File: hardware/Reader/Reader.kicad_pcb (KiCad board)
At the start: 4 copper layers, 53.3 x 125.1 mm, 126 parts, among them CN1 AHDF15A-KG-TAXB

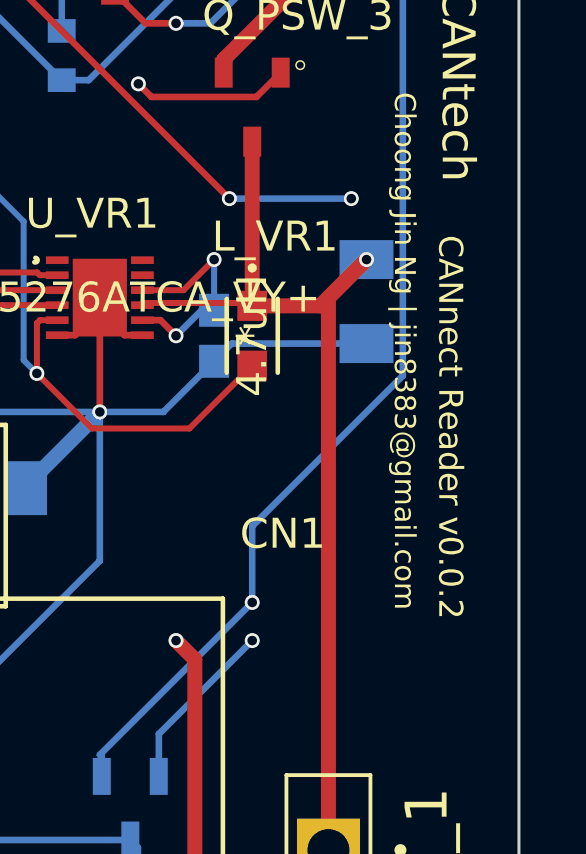
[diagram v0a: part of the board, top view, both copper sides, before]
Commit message: Updated version number for front silkscreen
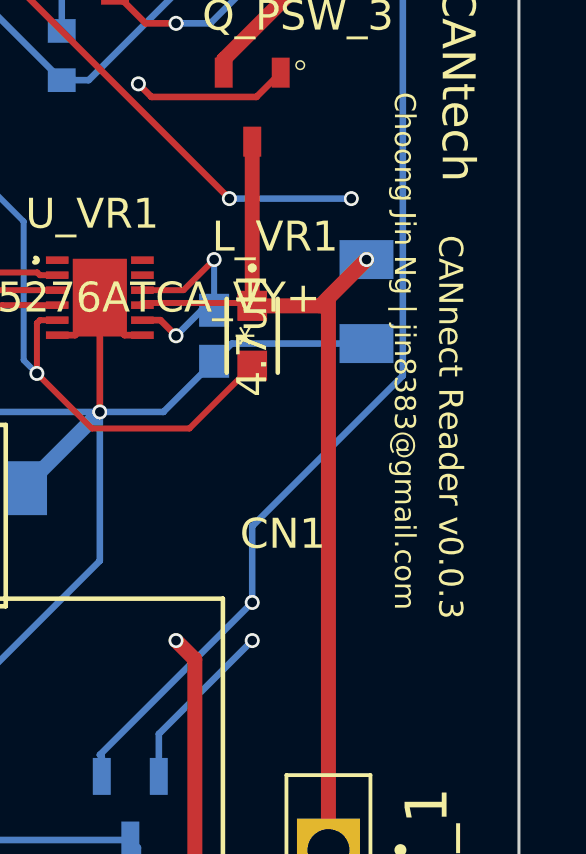
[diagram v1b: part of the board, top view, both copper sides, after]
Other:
- board text added: "CANnect Reader v0.0.3"
- board text removed: "CANnect Reader v0.0.2"
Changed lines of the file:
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@@
     (effects (font (size 1.1 1.1) (thickness 0.15)))
   )
-  (gr_text "CANnect Reader v0.0.2" (at 164.084 145.288 270) (layer F.SilkS)
+  (gr_text "CANnect Reader v0.0.3" (at 164.084 145.288 270) (layer F.SilkS)
     (effects (font (size 0.8 0.8) (thickness 0.15)))
   )

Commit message: Fixed a component name for header pin
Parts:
- C_SWCAN_2: value 4.7uF 25V -> 4.7uF

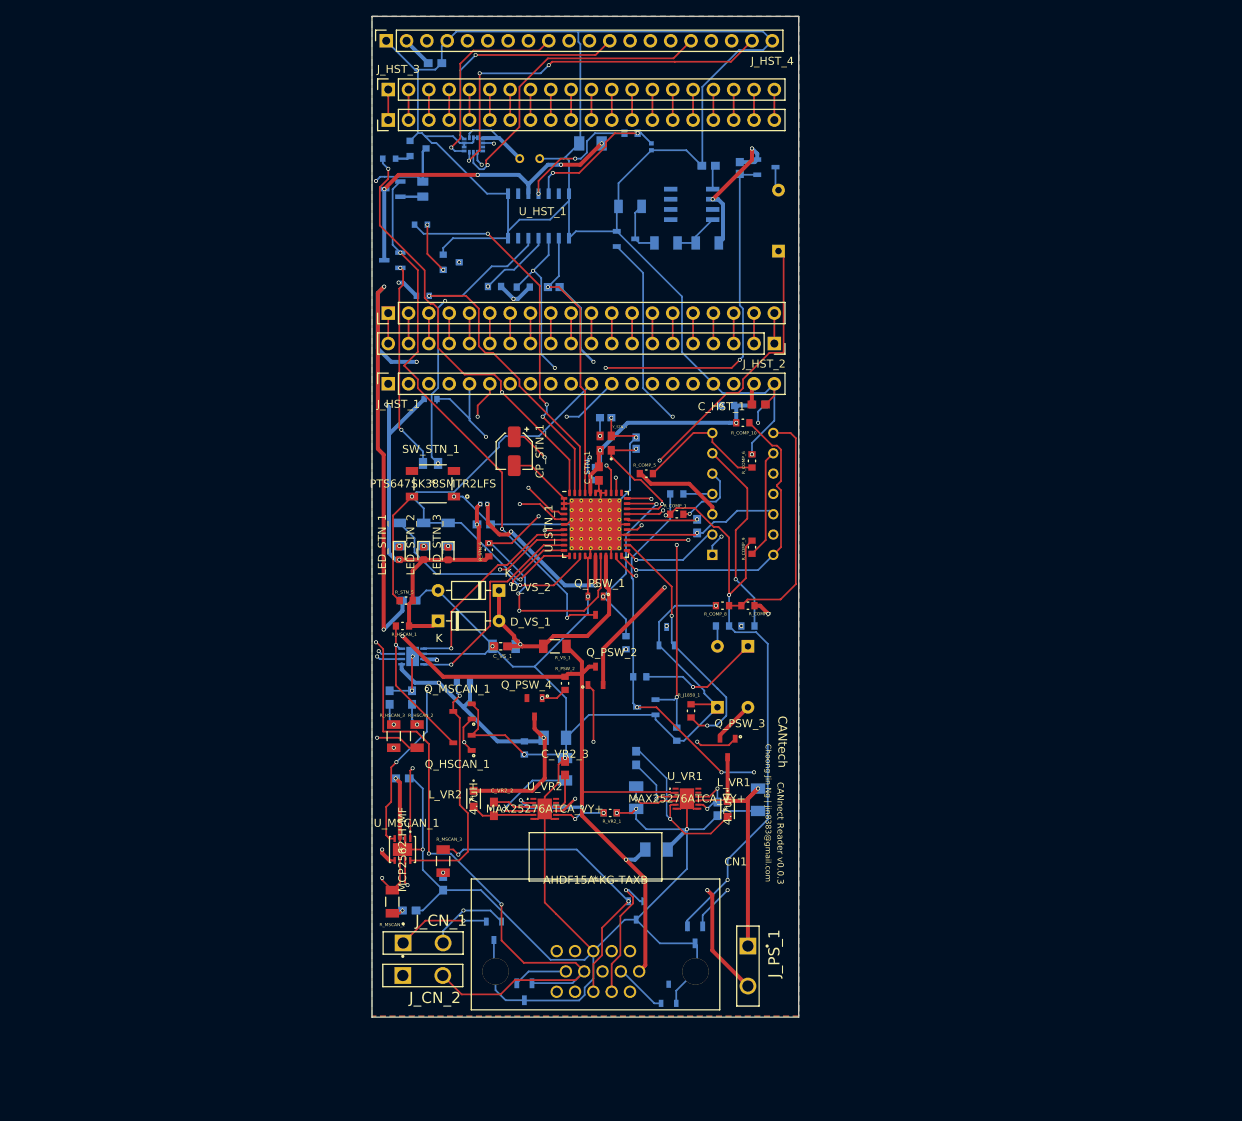
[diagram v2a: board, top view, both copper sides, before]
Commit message: Updated reader schematic to v0.0.5 by adding ESP32, removing unused transceivers, fixed design flaws, increased header pins and fixed footprints. Working on reader PCB design
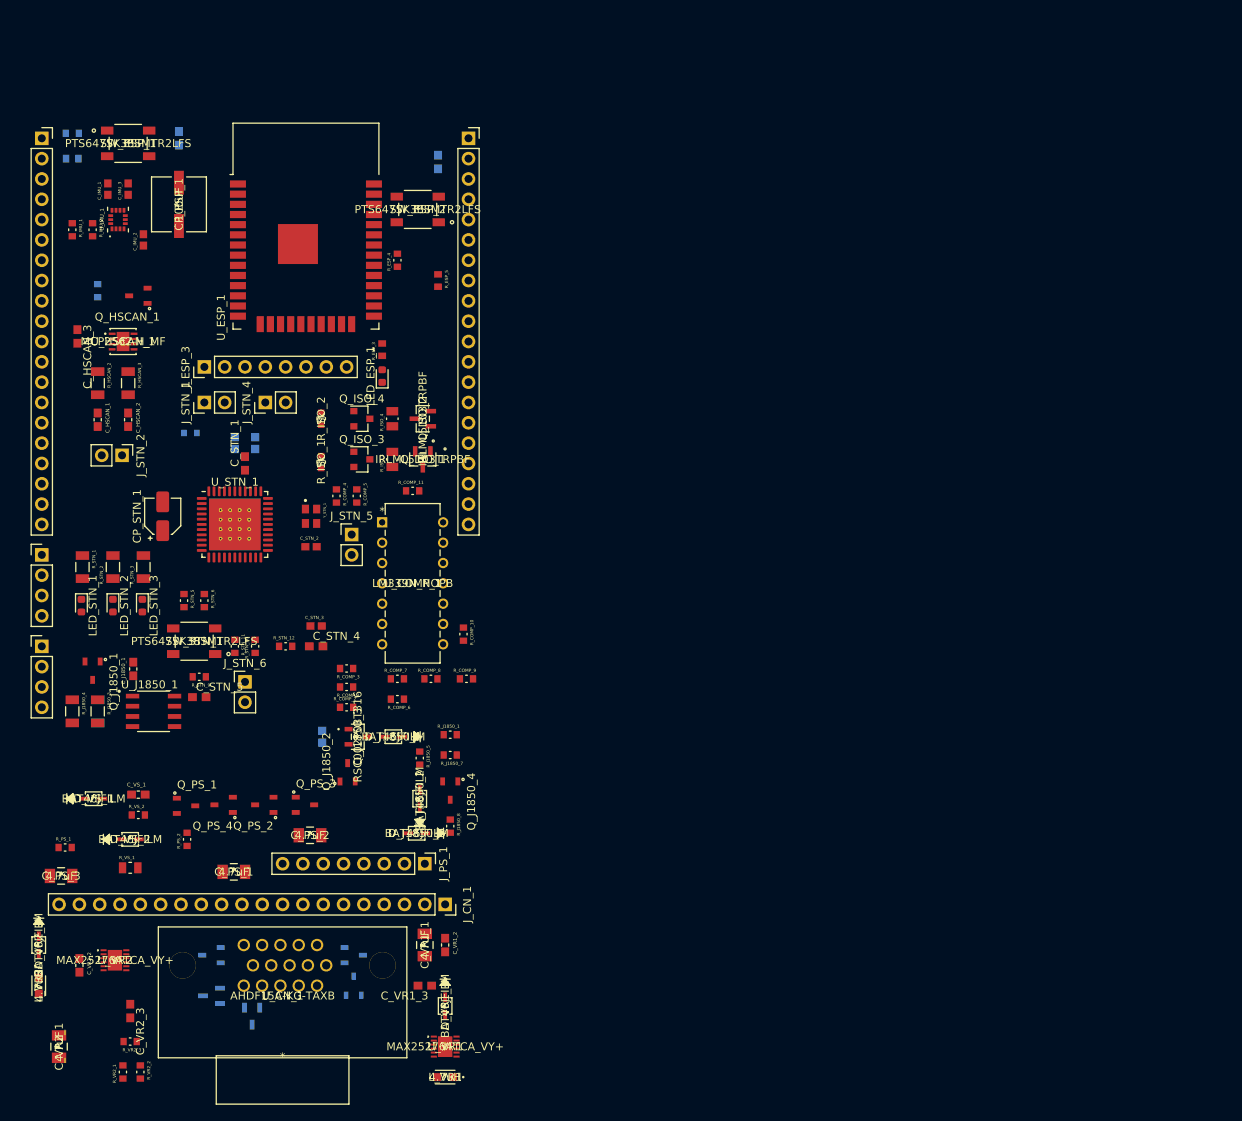
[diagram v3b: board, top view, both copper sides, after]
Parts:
- removed CN1: AHDF15A-KG-TAXB, footprints:AHDF15A-KG-TAXB
- removed C_HST_1, C_HST_2, C_MSCAN_3: 1uF, footprints:0603
- removed C_MM_1: 100nF, footprints:FA16C0G2A104JRU06
- removed C_MSCAN_1, C_MSCAN_2: 560pF, footprints:CAPC1608X90
- removed C_SWCAN_1: 150pF, footprints:CAPC1005X55N
- removed C_SWCAN_2: 4.7uF, footprints:C1206C475K3RACAUTO
- removed J_CN_2: 1546931-2, footprints:1546931-2
- removed J_HST_1, J_HST_2, J_HST_3, J_HST_4: 4157, Connector_PinSocket_2.54mm:PinSocket_1x20_P2.54mm_Vertical
- removed Q_MSCAN_1, Q_PSW_1, Q_PSW_2, Q_PSW_3, Q_PSW_4: NX7002AK,215, footprints:SOT95P230X110-3N
- removed R_COMP1, R_SWCAN_4, R_SWCAN_5: 10k, footprints:RESC1608X55N
- removed R_MSCAN_1, R_PSW_1, R_PSW_2: 100k, footprints:RESC1608X55N
- removed R_MSCAN_2, R_MSCAN_3: 100, footprints:RESC3216X70N
- removed R_SWCAN_3: 6.49k 0.12W, footprints:RESC1608X55N
- removed R_SWCAN_6: 1k, footprints:RC1608F102CS
- removed R_SWCAN_7: 1.5k, footprints:RESC1607X60N
- removed U_HST_1: ESP32_Holder, footprints:ESP32_Holder
- removed U_MM_1: LSM6DSMTR, footprints:PQFN50P300X250X86-14N
- removed U_MSCAN_1: MCP2562-H_MF, footprints:MCP2562-H&slash_MF
- removed U_SWCAN_1: TH8056KDC-AAA-014-RE, footprints:TH8056KDC-AAA-014-RE
- added CP_ESP_1: 100uF, footprints:UCB0J101MCL1GS, F.Cu at (88.9, 66.7)
- added C_ESP_1: 0.1uF, footprints:CAPC1608X90, B.Cu at (88.9, 58.4)
- added C_ESP_2: 0.1uF, footprints:CAPC1608X90, B.Cu at (121.3, 61.4)
- added C_IMU_1: 100nF, footprints:CAPC1608X90N, F.Cu at (80.0, 64.8)
- added C_IMU_2: 100nF, footprints:CAPC1608X90N, F.Cu at (84.5, 71.1)
- added C_IMU_3: 100nF, footprints:CAPC1608X90N, F.Cu at (82.5, 64.8)
- added D_VR1_1: BAT46JFILM, footprints:BAT46JFILM, F.Cu at (122.2, 166.9)
- added D_VR2_1: BAT46JFILM, footprints:BAT46JFILM, F.Cu at (71.4, 159.3)
- added J_ESP_1: 4157, Connector_PinSocket_2.54mm:PinSocket_1x20_P2.54mm_Vertical, F.Cu at (71.8, 58.4)
- added J_ESP_2: 4157, Connector_PinSocket_2.54mm:PinSocket_1x20_P2.54mm_Vertical, F.Cu at (125.1, 58.4)
- added J_ESP_3: Header_Pin_8, Connector_PinHeader_2.54mm:PinHeader_1x08_P2.54mm_Vertical, F.Cu at (92.1, 87.0)
- added J_OBD_1: Header_Pin_4, Connector_PinHeader_2.54mm:PinHeader_1x04_P2.54mm_Vertical, F.Cu at (71.8, 121.9)
- added J_OBD_2: Header_Pin_4, Connector_PinHeader_2.54mm:PinHeader_1x04_P2.54mm_Vertical, F.Cu at (71.8, 110.5)
- added J_STN_1: Header_Pin_2, Connector_PinHeader_2.54mm:PinHeader_1x02_P2.54mm_Vertical, F.Cu at (92.1, 91.4)
- added J_STN_2: Header_Pin_2, Connector_PinHeader_2.54mm:PinHeader_1x02_P2.54mm_Vertical, F.Cu at (81.8, 98.0)
- added J_STN_4: Header_Pin_2, Connector_PinHeader_2.54mm:PinHeader_1x02_P2.54mm_Vertical, F.Cu at (99.7, 91.4)
- added J_STN_5: Header_Pin_2, Connector_PinHeader_2.54mm:PinHeader_1x02_P2.54mm_Vertical, F.Cu at (110.5, 108.0)
- added J_STN_6: Header_Pin_2, Connector_PinHeader_2.54mm:PinHeader_1x02_P2.54mm_Vertical, F.Cu at (97.2, 126.4)
- added LED_ESP_1: LED, LED_SMD:LED_0603_1608Metric, F.Cu at (114.3, 88.1)
- added Q_PS_1: NX7002AK,215, footprints:SOT95P230X110-3N, F.Cu at (89.8, 141.9)
- added Q_PS_2: NX7002AK,215, footprints:SOT95P230X110-3N, F.Cu at (99.6, 141.7)
- added Q_PS_3: NX7002AK,215, footprints:SOT95P230X110-3N, F.Cu at (104.6, 141.7)
- added Q_PS_4: NX7002AK,215, footprints:SOT95P230X110-3N, F.Cu at (94.5, 141.7)
- added R_COMP_11: 10k, footprints:RESC1608X55N, F.Cu at (118.1, 102.5)
- added R_ESP_1: 10k, footprints:RESC1608X55N, B.Cu at (75.6, 57.8)
- added R_ESP_2: 500, footprints:RESC1508X55N, B.Cu at (75.6, 61.0)
- added R_ESP_3: 500, footprints:RESC1508X55N, F.Cu at (114.3, 84.8)
- added R_ESP_4: 10k, footprints:RESC1608X55N, F.Cu at (116.2, 73.7)
- added R_ESP_5: 500, footprints:RESC1508X55N, F.Cu at (121.3, 76.2)
- added R_IMU_1: 4.7k, footprints:RESC1608X55N, F.Cu at (75.6, 69.8)
- added R_IMU_2: 4.7k, footprints:RESC1608X55N, F.Cu at (78.1, 69.8)
- added R_PS_1: 100k, footprints:RESC1608X55N, F.Cu at (74.7, 147.1)
- added R_PS_2: 100k, footprints:RESC1608X55N, F.Cu at (89.9, 146.1)
- added R_STN_10: 10k, footprints:RESC1608X55N, F.Cu at (98.4, 121.9)
- added R_STN_11: 10, footprints:RESC1608X55N, F.Cu at (95.9, 121.9)
- added R_STN_12: 100k, footprints:RESC1608X55N, F.Cu at (102.2, 121.9)
- added R_STN_9: 100k, footprints:RESC1608X55N, F.Cu at (91.4, 125.7)
- added SW_ESP_1: PTS647SK38SMTR2LFS, footprints:PTS647SK38SMTR2LFS, F.Cu at (82.5, 59.1)
- added SW_ESP_2: PTS647SK38SMTR2LFS, footprints:PTS647SK38SMTR2LFS, F.Cu at (118.7, 67.3)
- added U_CN_1: AHDF15A-KG-TAXB, footprints:AHDF15A-KG-TAXB, F.Cu at (101.9, 165.6)
- added U_ESP_1: ESP32-WROOM-32D, footprints:CANtech-ESP32-WROOM-32, F.Cu at (104.8, 72.4)
- added U_IMU_1: LSM6DSMTR, footprints:PQFN50P300X250X86-14N, F.Cu at (81.3, 68.6)
- C_HSCAN_1, C_HSCAN_2, C_HSCAN_3, C_J1850_1, C_PS_1, C_PS_2, C_PS_3, C_STN_2, C_STN_3, C_STN_4, C_STN_5, C_VR1_1, C_VR1_2, C_VR1_3, C_VR2_1, Q_ISO_1, Q_ISO_2, Q_ISO_3, Q_ISO_4, Q_J1850_1, Q_J1850_2, Q_J1850_3, Q_J1850_4, R_COMP_2, R_COMP_3, R_COMP_4, R_ISO_1, R_ISO_2, R_J1850_3, R_J1850_4, R_J1850_5, R_J1850_7, R_J1850_8, R_STN_1, R_STN_2, R_VR2_2, R_VR2_3, U_COMP_1, U_HSCAN_1, U_J1850_1: moved to F.Cu
- D_J1850_1, D_J1850_2, D_J1850_3: value BAT46 -> BAT46JFILM; footprint Diode_THT:D_DO-35_SOD27_P7.62mm_Horizontal -> footprints:BAT46JFILM; moved to F.Cu
- D_VS_1, D_VS_2: value BAT46 -> BAT46JFILM; footprint Diode_THT:D_DO-35_SOD27_P7.62mm_Horizontal -> footprints:BAT46JFILM
- J_CN_1: value 1546931-2 -> 4157; footprint footprints:1546931-2 -> Connector_PinSocket_2.54mm:PinSocket_1x20_P2.54mm_Vertical
- J_PS_1: value 1546931-2 -> Header_Pin_8; footprint footprints:1546931-2 -> Connector_PinHeader_2.54mm:PinHeader_1x08_P2.54mm_Vertical
- LED_STN_1: value "Status" -> Status
- LED_STN_2: value "OBD Activity" -> OBD Activity
- LED_STN_3: value "Host Activity" -> Host Activity
- R_COMP_7: value 2.7k -> 10k
- R_COMP_8: value 10k -> 2.7k
- R_HSCAN_1: moved to B.Cu
- R_ISO_3, R_ISO_4: value 510k/0.5W -> 510k; footprint footprints:RESC2012X70N -> footprints:RESC2012X50N; moved to F.Cu
- R_STN_3: value 1k -> 330; footprint footprints:RC1608F102CS -> footprints:RESC3216X70N; moved to F.Cu
- R_STN_4: value 330 -> 1k; footprint footprints:RESC3216X70N -> footprints:RC1608F102CS
- R_STN_6: value 10k -> 100k
- R_STN_7: value 10 -> 1.5k; footprint footprints:RESC1005X40N -> footprints:RESC1607X60N
- R_STN_8: value 100k -> 1.5k; footprint footprints:RESC1608X55N -> footprints:RESC1607X60N
- R_VS_1: value 62k 1% -> 62k; footprint footprints:RESC3216X70N -> footprints:RESC2012X60N
- R_VS_2: value 10k 1% -> 10k; footprint footprints:RESC3216X70N -> footprints:RESC1608X55N; moved to F.Cu
- U_STN_1: footprint Package_DFN_QFN:QFN-44-1EP_8x8mm_P0.65mm_EP6.45x6.45mm_ThermalVias -> footprints:CANtech-STN2120-QFN-44-1EP_8x8mm
- moved R_J1850_6 96.1 mm to (78.7, 130.0), turned to 270 degrees
- moved C_J1850_1 95.5 mm to (83.2, 124.8), turned to 90 degrees
- moved R_J1850_4 94.0 mm to (75.6, 130.0), turned to 270 degrees
- moved U_J1850_1 92.4 mm to (85.7, 130.0), turned to 0 degrees
- moved R_J1850_3 92.1 mm to (78.7, 130.0), turned to 270 degrees
- moved R_J1850_2 88.2 mm to (106.8, 133.2), turned to 90 degrees
- moved Q_J1850_3 87.6 mm to (111.3, 133.2), turned to 270 degrees
- moved Q_J1850_1 85.8 mm to (78.1, 125.0), turned to 270 degrees
- moved D_J1850_1 77.5 mm to (115.7, 133.2), turned to 180 degrees
- moved C_VR2_1 72.1 mm to (73.9, 172.0), turned to 270 degrees
- moved Q_HSCAN_1 69.0 mm to (83.8, 78.1)
- moved R_VR2_1 69.0 mm to (81.9, 175.1), turned to 90 degrees
- moved R_VR2_2 67.1 mm to (84.1, 175.1), turned to 270 degrees
- moved C_PS_3 64.1 mm to (74.2, 150.6)
- moved C_VR2_3 62.3 mm to (82.8, 167.5), turned to 270 degrees
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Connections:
- net /Host/Analog_Voltage renamed /OBDII Interpreter/Analog_Voltage
- C_STN_4 pad 1: Net-(C_STN_4-Pad1) -> +3V3
- D_ESD_3 pad 3: Net-(D_ESD_3-Pad3) -> (no net)
- J_CN_1 pad 1: Pin6_ISO15765_CAN_BUS_High -> Pin13
- J_CN_1 pad 2: Pin14_ISO15765_CAN_BUS_Low -> Pin11_MS_CAN_Low
- J_PS_1 pad 2: +3V3 -> +5V_SW
- L_VR1 pad 1: +5V -> Net-(D_VR1_1-Pad2)
- L_VR2 pad 1: +3V3 -> Net-(D_VR2_1-Pad2)
- R_COMP_10 pad 1: +3V3 -> Net-(R_COMP_10-Pad1)
- R_COMP_10 pad 2: /OBDII Interpreter/Comparator Transceiver/VPW_RX -> Pin2_SAE_J1850_BUS+
- R_COMP_5 pad 1: +12V_SW -> +3V3
- R_COMP_5 pad 2: Net-(R_COMP_5-Pad2) -> /OBDII Interpreter/Comparator Transceiver/~ISO_RX~
- R_COMP_6 pad 1: Net-(R_COMP_5-Pad2) -> +12V_SW
- R_COMP_6 pad 2: Pin4_GnD_Chassis -> Net-(R_COMP_6-Pad2)
- R_COMP_7 pad 1: +5V_SW -> Net-(R_COMP_6-Pad2)
- R_COMP_7 pad 2: Net-(R_COMP_7-Pad2) -> Pin4_GnD_Chassis
- R_COMP_8 pad 1: Net-(R_COMP_7-Pad2) -> +5V_SW
- R_COMP_8 pad 2: Pin4_GnD_Chassis -> Net-(R_COMP_8-Pad2)
- R_COMP_9 pad 1: Net-(R_COMP_9-Pad1) -> Net-(R_COMP_8-Pad2)
- R_COMP_9 pad 2: Pin2_SAE_J1850_BUS+ -> Pin4_GnD_Chassis
- R_STN_2 pad 2: /OBDII Interpreter/~RESET_OBD_HW~ -> /Host/~RESET_OBD_HW~
- R_STN_3 pad 1: +3V3 -> Net-(LED_STN_3-Pad1)
- R_STN_3 pad 2: /Host/HOST_TX -> /OBDII Interpreter/OBDII Chip/~HOST_ACT_LED~
- R_STN_4 pad 1: Net-(LED_STN_3-Pad1) -> +3V3
- R_STN_4 pad 2: /OBDII Interpreter/~RESET_OBD_HW~ -> /Host/HST_TX
- R_STN_5 pad 1: /OBDII Interpreter/~RESET_OBD_HW~ -> Net-(R_STN_5-Pad1)
- R_STN_6 pad 1: +3V3 -> Net-(R_STN_6-Pad1)
- R_STN_6 pad 2: /OBDII Interpreter/RESET_OBD_SW -> +3V3
- R_STN_7 pad 2: VDDA -> Net-(R_STN_7-Pad2)
- R_STN_8 pad 2: /Host/~RESET_OBD_HW~ -> Net-(R_STN_8-Pad2)
- R_VR2_3 pad 1: +3V3 -> Net-(D_VR2_1-Pad2)
- R_VR2_3 pad 2: Pin4_GnD_Chassis -> Net-(R_VR2_1-Pad2)
- SW_STN_1 pad 1: Pin4_GnD_Chassis -> Net-(R_STN_9-Pad1)
- SW_STN_1 pad 2: /OBDII Interpreter/~RESET_OBD_HW~ -> /Host/~RESET_OBD_HW~
- SW_STN_1 pad 3: Net-(SW_STN_1-Pad3) -> Pin4_GnD_Chassis
- SW_STN_1 pad 4: Net-(SW_STN_1-Pad4) -> (no net)
- U_COMP_1 pad 10: Net-(U_COMP_1-Pad10) -> (no net)
- U_COMP_1 pad 11: Net-(U_COMP_1-Pad11) -> (no net)
- U_COMP_1 pad 13: Net-(U_COMP_1-Pad13) -> (no net)
- U_COMP_1 pad 7: Net-(R_COMP_5-Pad2) -> Net-(R_COMP_6-Pad2)
- U_COMP_1 pad 8: Net-(R_COMP_7-Pad2) -> Net-(R_COMP_8-Pad2)
- U_COMP_1 pad 9: Net-(R_COMP_9-Pad1) -> Net-(R_COMP_10-Pad1)
- U_J1850_1 pad 3: Net-(U_J1850_1-Pad3) -> (no net)
- U_J1850_1 pad 5: Net-(U_J1850_1-Pad5) -> (no net)
- U_J1850_1 pad 6: Net-(U_J1850_1-Pad6) -> (no net)
- U_J1850_1 pad 7: Net-(U_J1850_1-Pad7) -> (no net)
- U_J1850_1 pad 8: Net-(U_J1850_1-Pad8) -> (no net)
- U_STN_1 pad 11: /OBDII Interpreter/Medium Speed CAN Transceiver/MS_CAN_RX -> Net-(R_STN_6-Pad1)
- U_STN_1 pad 12: /OBDII Interpreter/~RESET_OBD_HW~ -> /Host/~RESET_OBD_HW~
- U_STN_1 pad 27: /Host/~RESET_OBD_HW~ -> /Host/~SLEEP_OBD~
- U_STN_1 pad 28: Pin4_GnD_Chassis -> +3V3
- U_STN_1 pad 29: Net-(C_STN_4-Pad1) -> Pin4_GnD_Chassis
- U_STN_1 pad 34: /OBDII Interpreter/OBDII Chip/SW_CAN_LOAD -> (no net)
- U_STN_1 pad 35: /OBDII Interpreter/OBDII Chip/SW_CAN_MODE0 -> (no net)
- U_STN_1 pad 36: /OBDII Interpreter/OBDII Chip/SW_CAN_MODE1 -> (no net)
- U_STN_1 pad 4: /Host/HOST_TX -> /Host/HST_TX
- U_STN_1 pad 41: /OBDII Interpreter/OBDII Chip/SW_CAN_TX -> Net-(R_STN_8-Pad2)
- U_STN_1 pad 42: /OBDII Interpreter/OBDII Chip/SW_CAN_RX -> Net-(R_STN_7-Pad2)
- U_STN_1 pad 5: /Host/HOST_RX -> /Host/HST_RX
- U_STN_1 pad 9: /OBDII Interpreter/Medium Speed CAN Transceiver/MS_CAN_TX -> Net-(R_STN_5-Pad1)
- U_VR1 pad 1: /Power Supply/Voltage Regulator (5V)/Spread_Spectrum_Enable -> (no net)
- U_VR1 pad 11: /Power Supply/Voltage Regulator (5V)/Sync_Signal -> (no net)
- U_VR1 pad 12: /Power Supply/Voltage Regulator (5V)/PGood -> (no net)
- U_VR1 pad 9: +5V -> Net-(D_VR1_1-Pad2)
- U_VR2 pad 1: /Power Supply/Voltage Regulator (3.3V)/Spread_Spectrum_Enable -> (no net)
- U_VR2 pad 11: /Power Supply/Voltage Regulator (3.3V)/Sync_Signal -> (no net)
- U_VR2 pad 12: /Power Supply/Voltage Regulator (3.3V)/PGood -> (no net)
- U_VR2 pad 9: +3V3 -> Net-(D_VR2_1-Pad2)
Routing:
- net Pin4_GnD_Chassis: track 659.3 -> 0.00 mm, vias 17 -> 0
- net +3V3: track 311.3 -> 0.00 mm, vias 13 -> 0
- net +5V: track 272.5 -> 0.00 mm, vias 7 -> 0
- net Pin16_Raw_+12V_Battery: track 194.3 -> 0.00 mm, vias 8 -> 0
- net Pin7_ISO9141_K-Line: track 164.0 -> 0.00 mm, vias 4 -> 0
- net Pin15_ISO9141_L-Line: track 155.2 -> 0.00 mm, vias 4 -> 0
- net Pin1_SW_CAN: track 146.6 -> 0.00 mm, vias 2 -> 0
- net Pin2_SAE_J1850_BUS+: track 144.3 -> 0.00 mm, vias 4 -> 0
- net /OBDII Interpreter/PWR_CTRL: track 118.5 -> 0.00 mm, vias 6 -> 0
- net +5V_SW: track 100.8 -> 0.00 mm, vias 2 -> 0
- net Pin10_SAE_J1850_BUS-: track 93.7 -> 0.00 mm, vias 4 -> 0
- net Pin14_ISO15765_CAN_BUS_Low: track 85.4 -> 0.00 mm, vias 3 -> 0
- net Net-(Q_J1850_2-Pad3): track 79.6 -> 0.00 mm, vias 3 -> 0
- net /Host/~PWR_CTRL~: track 72.2 -> 0.00 mm, vias 3 -> 0
- net /OBDII Interpreter/Analog_Voltage: track 70.5 -> 0.00 mm, vias 1 -> 0
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- removed copper zone on In2.Cu, net +3V3
- removed copper zone on In1.Cu, net +5V
- removed copper zone on B.Cu, net Pin4_GnD_Chassis
- removed copper zone on F.Cu, net Pin4_GnD_Chassis
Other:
- board outline removed
- net class Default: trace_width 0.22 -> 0.2; via_dia 0.5 -> 0.6
- net class Power: via_dia 0.5 -> 0.6
- rule via_min_size: 0.5 -> 0.6
- board text removed: "CANnect Reader v0.0.3"
- board text removed: "CANtech"
- board text removed: "Choong Jin Ng | jin8383@gmail.com"
